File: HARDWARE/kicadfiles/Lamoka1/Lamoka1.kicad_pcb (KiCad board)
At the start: 2 copper layers, 38 parts, among them J1 2606-1108/010-000, J2 2606-1352, J3 USB_C_Receptacle_USB2.0_14P, J4 470531000, J5 2604-1103, U1 RP2354A, U10 ADS7128IRTER, U3 74AHCT1G125, U7 TPS62160DSGR, U8 TMP235A2DBZR, U9 TMP235A2DBZR

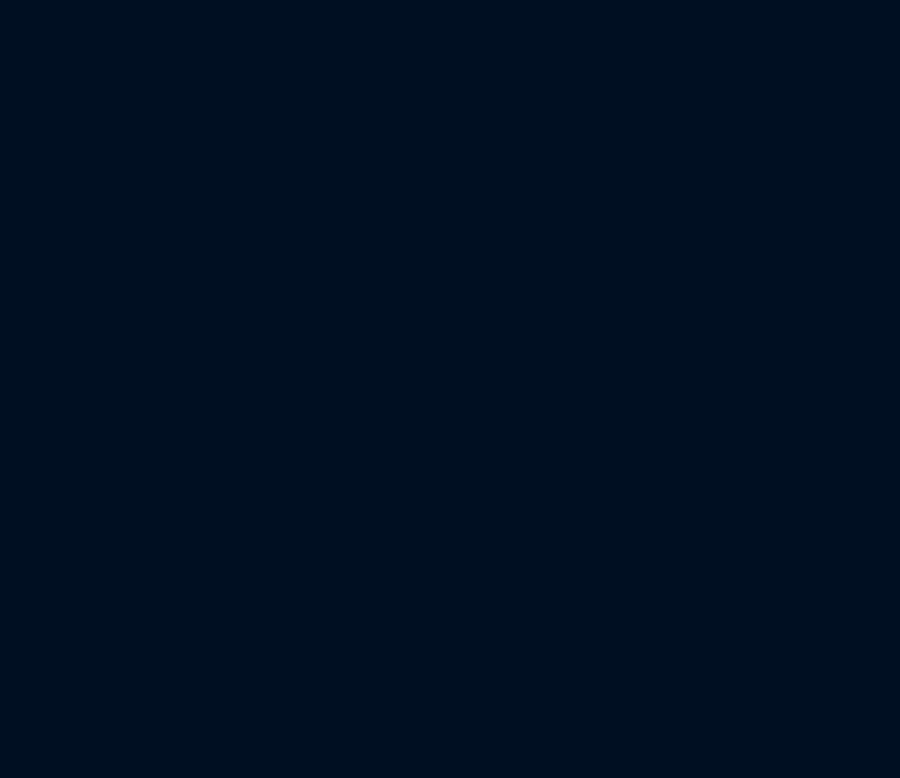
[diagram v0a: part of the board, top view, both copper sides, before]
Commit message: ADD source current monitoring, and other features, some more correcting of MPN and footprints
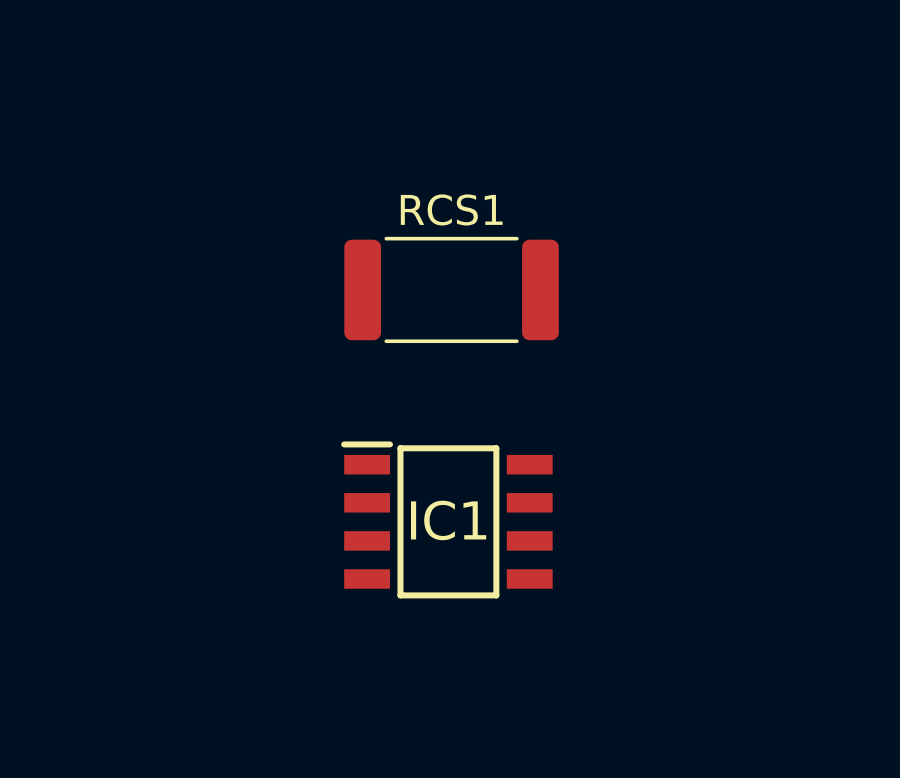
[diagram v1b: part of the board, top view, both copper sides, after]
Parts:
- added IC1: INA240A2DR, INA240A2DR:SOIC127P600X175-8N, F.Cu at (211.2, 119.7)
- added RCS1: 2m, Resistor_SMD:R_2512_6332Metric, F.Cu at (211.3, 112.0)
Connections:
- C24 pad 1: /11-14V input -> /Inversion-Section/CSP
- U10 pad 3: unconnected-(U10-AIN4/GPIO4-Pad3) -> /Control-Section/AIN4
- U7 pad 2: /11-14V input -> /Inversion-Section/CSP
- U7 pad 3: /11-14V input -> /Inversion-Section/CSP

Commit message: General work on schem, BOM, footprints. Rout 11-14v to 5v buck converter
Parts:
- C24: value TMK212BBJ106KG -> 10uF; footprint TMK212BBJ106KG:CAP_TMK212_TAY -> TMK212BBJ106KG-T:CAPC2114X145N
- C25: value GRM31CR71A226KE15L -> 22uF
- L3: value PA4332.222NLT -> 2.2uH, 4.3A
- R19: value RC0603FR-07180KL -> 180k
- R20: value CRCW0402953KFKED -> 953k
- R21: value CRCW0402100KFKED -> 100k
- moved C24 205.9 mm to (44.9, 76.9), turned to 180 degrees
- moved U7 194.6 mm to (48.2, 76.8)
- moved L3 181.4 mm to (52.9, 77.0), turned to 90 degrees
- moved R19 178.5 mm to (50.1, 81.5), turned to -90 degrees
- moved R21 176.6 mm to (51.7, 73.8), turned to 180 degrees
- moved R20 162.8 mm to (52.2, 80.7), turned to 180 degrees
- moved C25 120.2 mm to (55.2, 81.8), turned to 90 degrees
- moved C21 65.9 mm to (219.0, 93.8)
- moved R5 65.9 mm to (200.9, 119.0)
- moved RCS1 65.9 mm to (277.1, 115.5)
- moved U1 65.9 mm to (213.8, 62.5)
- moved U8 65.9 mm to (274.1, 43.8)
- moved U9 65.9 mm to (261.9, 54.7)
- moved J5 65.9 mm to (191.5, 38.7)
- moved C11 65.9 mm to (196.8, 90.9)
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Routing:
- net /Buck-5v: track 0.00 -> 26.1 mm
- net GND: track 0.00 -> 26.0 mm
- net /11-14V input: track 0.00 -> 12.5 mm
- net Net-(U7-FB): track 0.00 -> 5.09 mm
- net Net-(U7-SW): track 0.00 -> 4.13 mm
- net /Control-Section/PG: track 0.00 -> 3.36 mm
- net /Inversion-Section/CSP: track 0.00 -> 3.35 mm

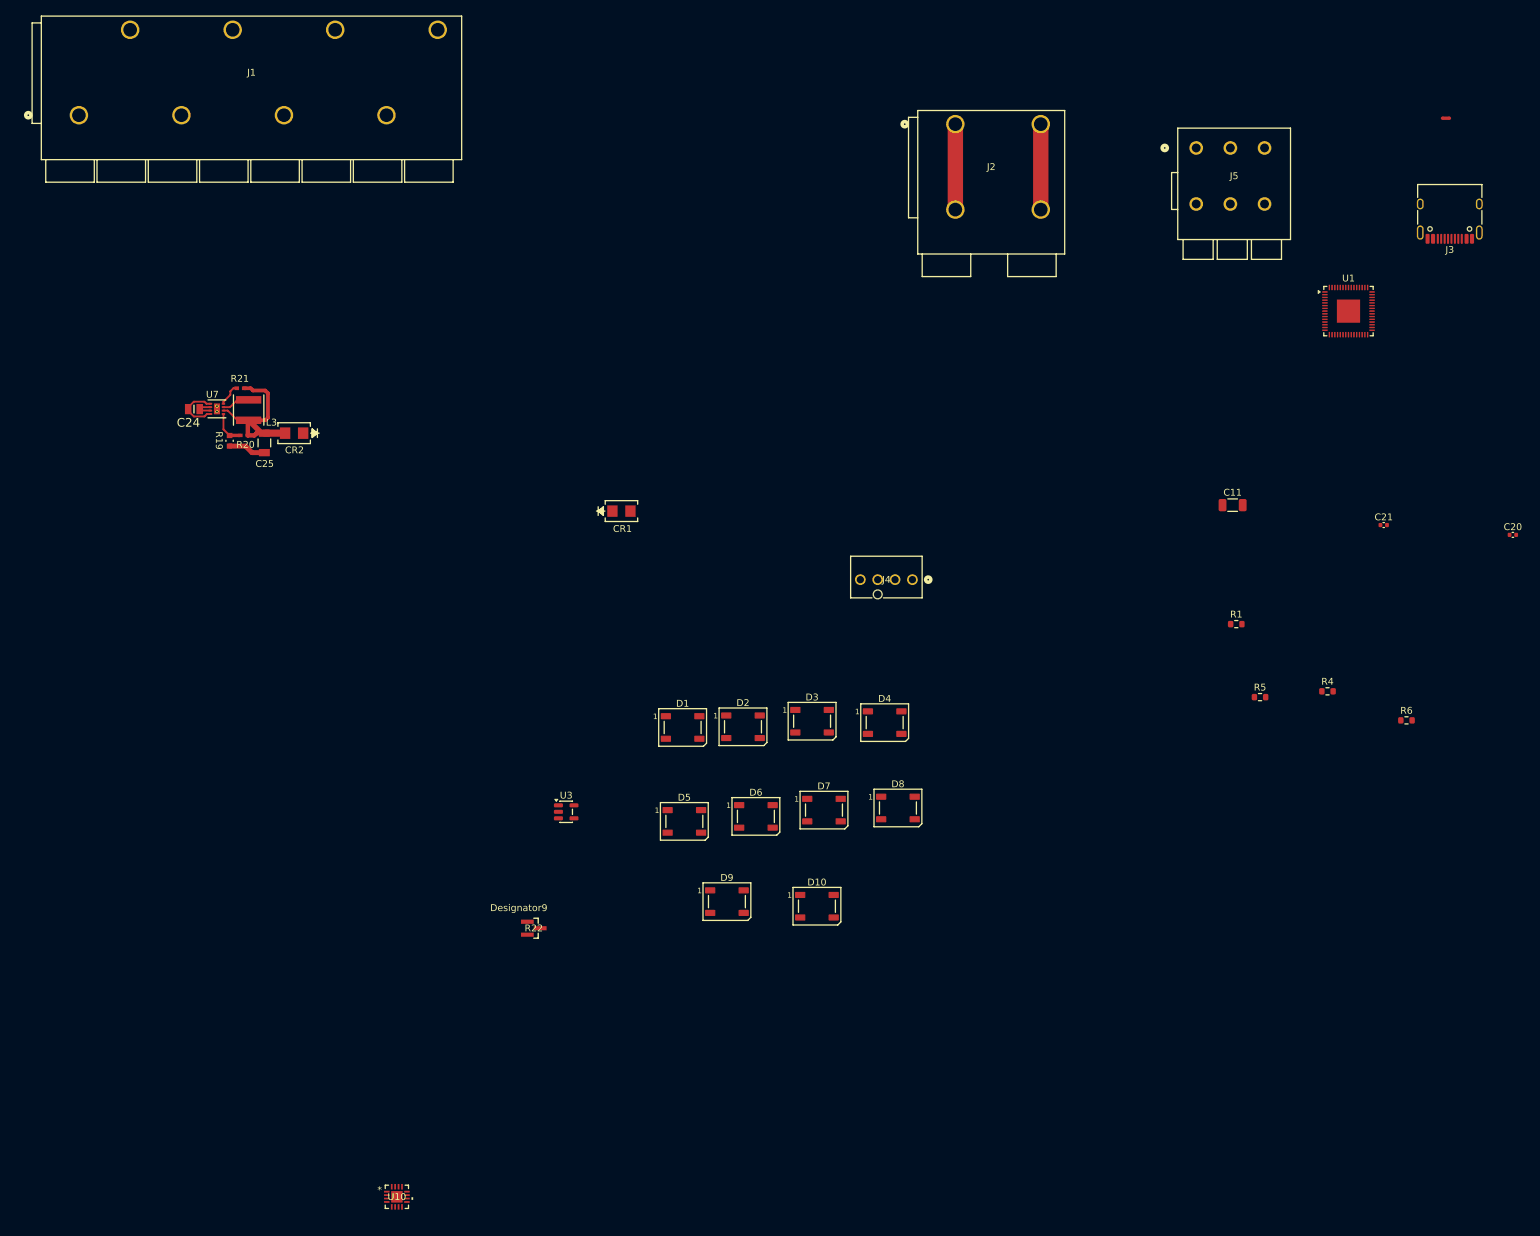
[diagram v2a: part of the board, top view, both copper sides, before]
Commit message: Improving documentation, some more routing
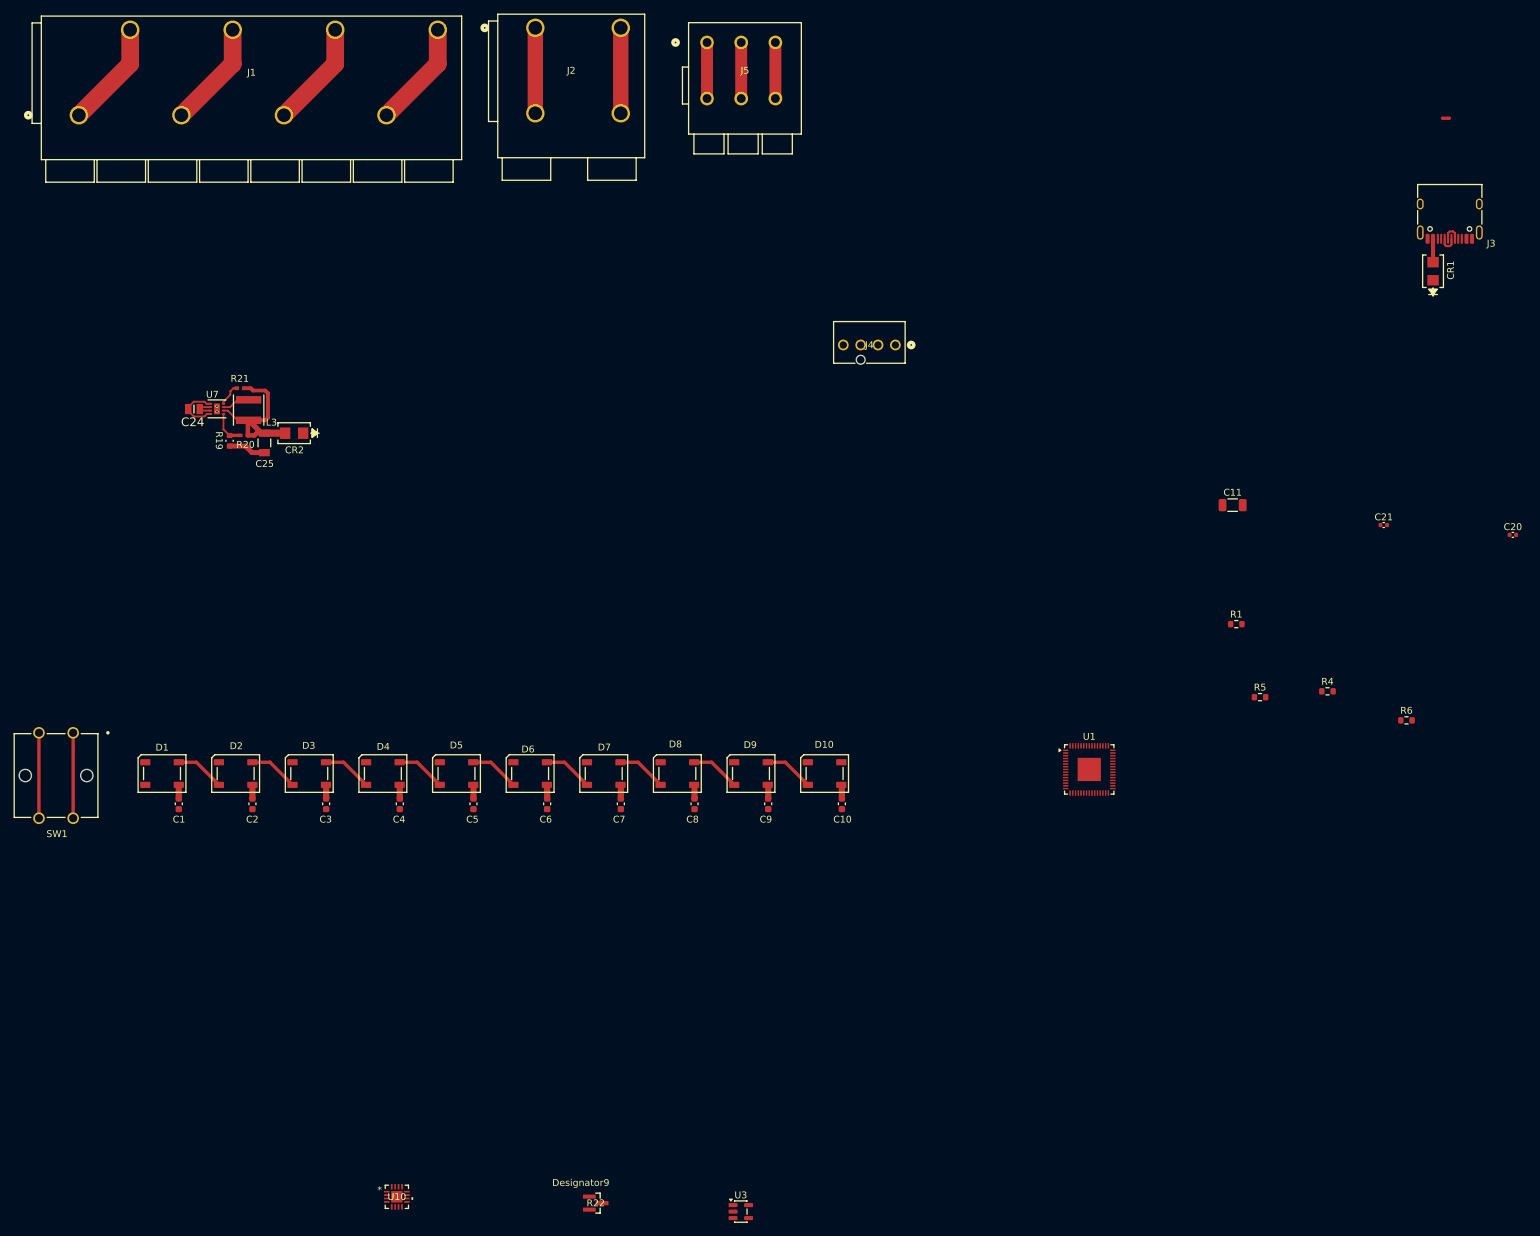
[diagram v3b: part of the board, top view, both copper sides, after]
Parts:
- added C1: 100n, Capacitor_SMD:C_0603_1608Metric, F.Cu at (42.7, 134.6)
- added C10: 100n, Capacitor_SMD:C_0603_1608Metric, F.Cu at (139.7, 134.6)
- added C2: 100n, Capacitor_SMD:C_0603_1608Metric, F.Cu at (53.4, 134.6)
- added C3: 100n, Capacitor_SMD:C_0603_1608Metric, F.Cu at (64.2, 134.6)
- added C4: 100n, Capacitor_SMD:C_0603_1608Metric, F.Cu at (75.0, 134.6)
- added C5: 100n, Capacitor_SMD:C_0603_1608Metric, F.Cu at (85.8, 134.6)
- added C6: 100n, Capacitor_SMD:C_0603_1608Metric, F.Cu at (96.6, 134.6)
- added C7: 100n, Capacitor_SMD:C_0603_1608Metric, F.Cu at (107.3, 134.6)
- added C8: 100n, Capacitor_SMD:C_0603_1608Metric, F.Cu at (118.1, 134.6)
- added C9: 100n, Capacitor_SMD:C_0603_1608Metric, F.Cu at (128.9, 134.6)
- added SW1: B3F-4055, B3F-4055:SW_B3F-4050_OMR, F.Cu at (27.2, 124.2)
- moved CR1 123.8 mm to (226.2, 56.7), turned to 90 degrees
- moved U1 77.0 mm to (175.9, 129.6)
- moved D1 76.5 mm to (40.2, 130.2), turned to 180 degrees
- moved D2 74.5 mm to (51.0, 130.2), turned to 180 degrees
- moved D3 74.0 mm to (61.8, 130.2), turned to 180 degrees
- moved D4 73.8 mm to (72.5, 130.2), turned to 180 degrees
- moved J5 73.2 mm to (120.0, 23.2)
- moved U3 63.8 mm to (124.9, 194.3)
- moved J2 63.0 mm to (94.8, 21.1)
- moved R22 41.2 mm to (103.7, 193.0)
- moved J4 34.4 mm to (147.5, 67.5)
- moved D5 34.1 mm to (83.3, 130.2), turned to 180 degrees
- moved D6 33.6 mm to (94.1, 130.2), turned to 180 degrees
- moved D7 32.7 mm to (104.8, 130.2), turned to 180 degrees
- moved D8 32.7 mm to (115.6, 130.2), turned to 180 degrees
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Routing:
- net /RED: track 0.00 -> 23.8 mm
- net /BLACK: track 0.00 -> 23.8 mm
- net GND: track 26.0 -> 46.7 mm
- net /Control-Section/5V: track 0.00 -> 20.2 mm
- net /BROWN: track 0.00 -> 15.6 mm
- net /BLUE: track 0.00 -> 15.6 mm
- net /Control-Section/BTN: track 0.00 -> 12.5 mm
- net Net-(D5-DOUT): track 0.00 -> 7.24 mm
- net Net-(D1-DOUT): track 0.00 -> 7.24 mm
- net Net-(D8-DOUT): track 0.00 -> 7.24 mm
- net Net-(D7-DOUT): track 0.00 -> 7.24 mm
- net Net-(D6-DOUT): track 0.00 -> 7.24 mm
- net Net-(D4-DOUT): track 0.00 -> 7.24 mm
- net Net-(D2-DOUT): track 0.00 -> 7.24 mm
- net Net-(D3-DOUT): track 0.00 -> 7.24 mm
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
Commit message: ADD seperate user interface board, improve doccumentation
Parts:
- removed R22: 10k, TMP235A2DBZR:DBZ0003A-IPC_A
- added C12: 10u, Capacitor_SMD:C_0402_1005Metric, F.Cu at (47.1, 122.2)
- added C13: 10u, Capacitor_SMD:C_0402_1005Metric, F.Cu at (44.9, 117.5)
- added C31: 100nF, Capacitor_SMD:C_0603_1608Metric, F.Cu at (73.0, 160.4)
- added J6: Male-Header, Connector_PinHeader_2.54mm:PinHeader_1x05_P2.54mm_Vertical_SMD_Pin1Left, B.Cu at (38.7, 44.4)
- added J7: Male-Header, Connector_PinHeader_2.54mm:PinHeader_1x05_P2.54mm_Vertical_SMD_Pin1Left, F.Cu at (116.3, 86.0)
- added R2: 5.1k, RC0603FR-07180KL:RC0603N_YAG, F.Cu at (39.3, 106.1)
- added R3: 5.1k, RC0603FR-07180KL:RC0603N_YAG, F.Cu at (39.3, 111.0)
- added R33: 22, Resistor_SMD:R_0603_1608Metric, F.Cu at (73.0, 157.3)
- added R9: 10k, Resistor_SMD:R_0603_1608Metric, F.Cu at (33.5, 37.7)
- added U2: AMS1117-3.3, Package_TO_SOT_SMD:SOT-223-3_TabPin2, F.Cu at (50.3, 117.5)
- added U4: LM5122MH/NOPB, LM5122QMHX-NOPB:PWP20_3P0X4P2, F.Cu at (147.0, 178.8)
- moved U8 214.2 mm to (72.1, 115.1)
- moved J3 205.6 mm to (32.3, 109.0), turned to -90 degrees
- moved IC1 204.1 mm to (74.9, 151.9), turned to -90 degrees
- moved CR1 195.9 mm to (39.4, 115.8)
- moved RCS1 193.5 mm to (87.1, 152.0), turned to 90 degrees
- moved R6 183.4 mm to (39.4, 109.4)
- moved U3 177.9 mm to (43.1, 36.3), turned to 90 degrees
- moved C11 175.0 mm to (28.8, 42.1), turned to 180 degrees
- moved R1 171.0 mm to (44.1, 32.5), turned to -90 degrees
- moved R5 161.9 mm to (39.4, 107.7)
- moved J2 138.7 mm to (87.1, 159.6)
- moved U9 106.9 mm to (160.4, 88.2)
- moved SW1 102.3 mm to (33.5, 22.1)
- moved C1 102.3 mm to (49.0, 32.5)
- moved C10 102.3 mm to (146.0, 32.5)
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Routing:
- net /Control-Section/AIN4: track 0.00 -> 46.9 mm
- net GND: track 46.7 -> 2.41 mm, vias 0 -> 1
- net /Control-Section/USB_DP: track 0.00 -> 39.2 mm
- net /Control-Section/USB_DM: track 0.00 -> 38.7 mm
- net /User-Interface-Section/BTN: track 0.00 -> 29.7 mm, vias 0 -> 1
- net /Control-Section/5V: track 20.2 -> 45.9 mm
- net /Control-Section/3v3: track 0.00 -> 21.6 mm
- net /11-14V input: track 12.5 -> 27.6 mm
- net /Inversion-Section/CSP: track 3.35 -> 15.0 mm
- net /Control-Section/GPIO11: track 0.00 -> 9.68 mm, vias 0 -> 1
- net /User-Interface-Section/3v3: track 0.00 -> 9.01 mm, vias 0 -> 1
- net /Control-Section/USB-5v: track 3.42 -> 12.4 mm
- net /Control-Section/GPIO9: track 0.00 -> 7.55 mm
- net /Control-Section/GPIO8: track 0.00 -> 7.51 mm
- net /User-Interface-Section/5V: track 0.00 -> 6.18 mm, vias 0 -> 1
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- added copper zone on F.Cu, net /Control-Section/5V
- added copper zone on B.Cu, net GND
- added copper zone on F.Cu, net GND
